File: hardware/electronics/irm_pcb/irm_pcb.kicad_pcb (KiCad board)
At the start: 2 copper layers, 64 parts, among them IC1 23LC1024, J1 Conn_01x04, J10 Conn_02x05_Counter_Clockwise, J11 Conn_01x04, J12 Conn_01x06, J13 Conn_01x06, J14 Conn_01x10, J16 Screw_Terminal_01x02, J17 Conn_01x06, J2 JUMPER_OPEN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

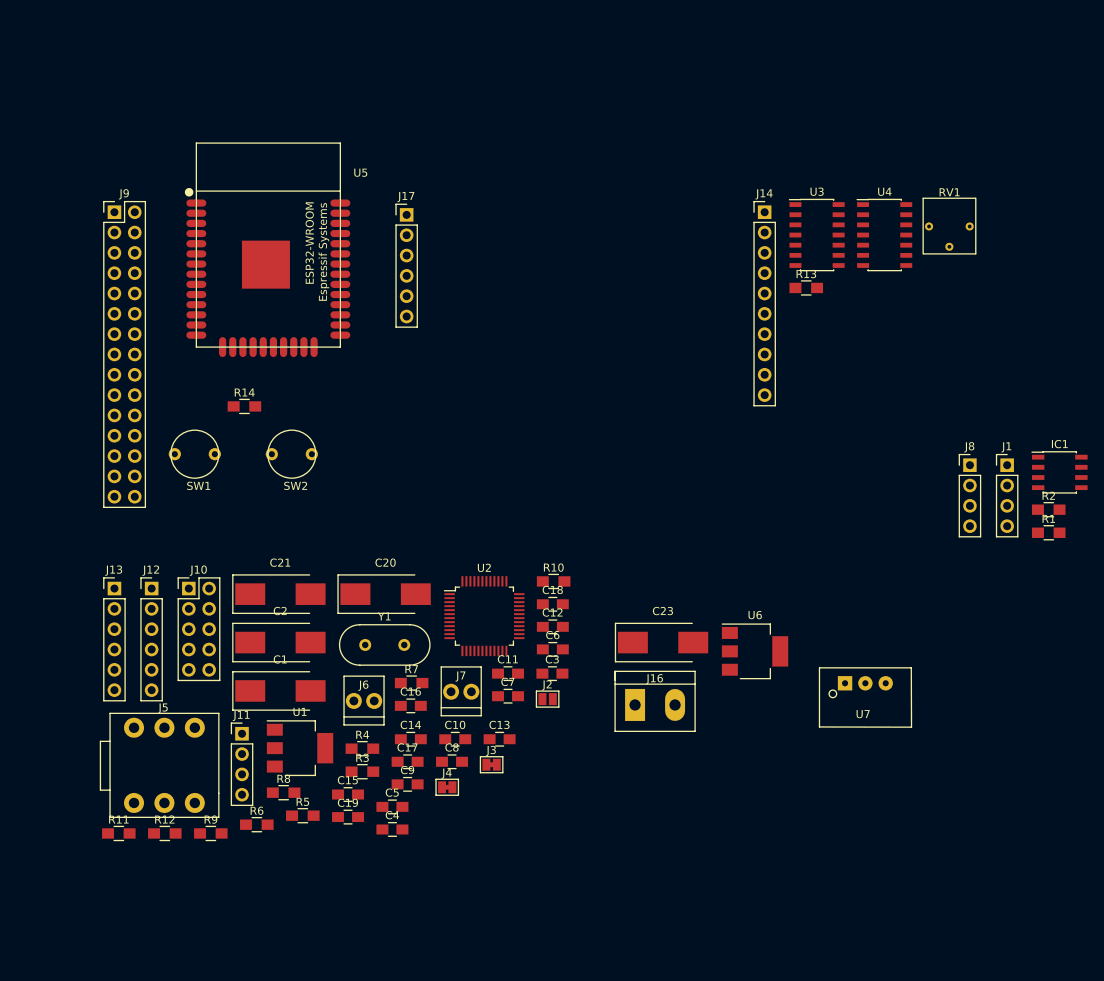
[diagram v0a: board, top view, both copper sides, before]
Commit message: New borad layout - routing incomplete
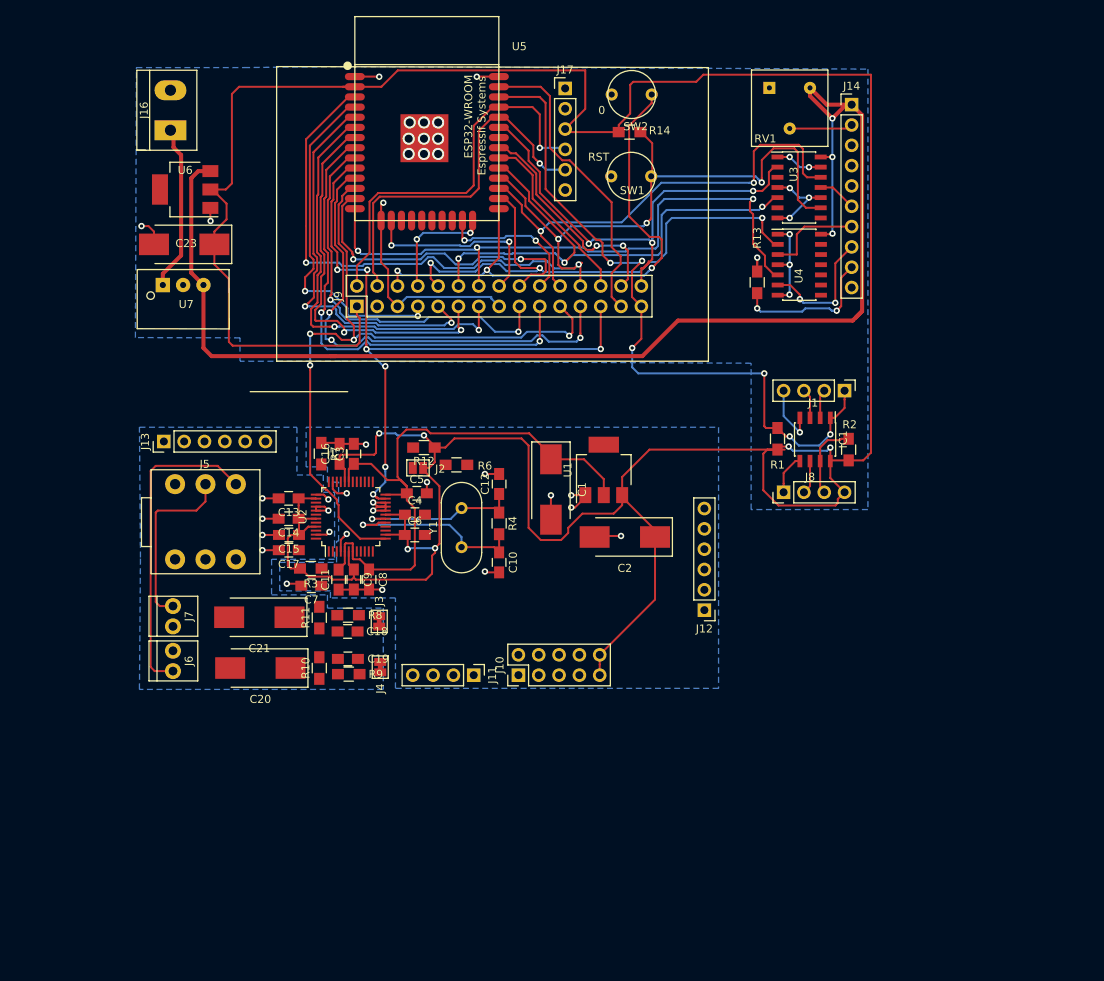
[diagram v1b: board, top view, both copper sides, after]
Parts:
- removed R5: 100K, Resistors_SMD:R_0805_HandSoldering
- RV1: footprint irm_pcb:Potentiometer_Trimmer_Bourns_3339H_Horizontal -> irm_pcb:Potentiometer_Trimmer_Bourns_3386F
- moved U7 98.7 mm to (84.3, 43.1)
- moved J16 95.8 mm to (84.6, 21.2), turned to 90 degrees
- moved U6 91.7 mm to (87.1, 31.1), turned to 180 degrees
- moved C23 77.9 mm to (87.0, 38.0), turned to 180 degrees
- moved J12 69.1 mm to (152.0, 83.7), turned to 180 degrees
- moved SW1 64.7 mm to (142.9, 29.5)
- moved SW2 61.9 mm to (142.9, 19.2)
- moved R14 59.1 mm to (142.7, 23.9)
- moved R12 58.1 mm to (117.0, 63.4), turned to 180 degrees
- moved U1 51.5 mm to (139.4, 66.2), turned to 90 degrees
- moved R6 51.4 mm to (121.0, 65.5), turned to 180 degrees
- moved C2 45.0 mm to (142.1, 74.5), turned to 180 degrees
- moved J10 42.6 mm to (128.8, 91.8), turned to 90 degrees
- moved C1 42.2 mm to (132.8, 68.6), turned to 270 degrees
- moved C13 40.0 mm to (100.1, 69.7), turned to 180 degrees
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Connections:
- net Net-(J16-Pad1) renamed +24V
- J7 pad 1: AGND -> /MP3 Codec/R_OUT
- J7 pad 2: /MP3 Codec/R_OUT -> AGND
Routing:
- net +3V3: track 0.00 -> 420.3 mm, vias 0 -> 6
- net +5V: track 0.00 -> 169.4 mm, vias 0 -> 3
- net /Control/EN: track 0.00 -> 137.2 mm, vias 0 -> 5
- net AGND: track 0.00 -> 136.2 mm, vias 0 -> 45
- net /MP3 Codec/XDCS: track 0.00 -> 91.4 mm, vias 0 -> 4
- net /Buffer RAM/RAM-CS: track 0.00 -> 88.4 mm, vias 0 -> 7
- net /MP3 Codec/XCS: track 0.00 -> 84.7 mm, vias 0 -> 7
- net /Control/RS: track 0.00 -> 77.5 mm, vias 0 -> 3
- net +1.8V: track 0.00 -> 75.9 mm
- net /WROOM Processor/IO0: track 0.00 -> 68.9 mm, vias 0 -> 3
- net /Control/D5: track 0.00 -> 68.3 mm, vias 0 -> 3
- net /Control/D6: track 0.00 -> 66.9 mm, vias 0 -> 3
- net /Control/D4: track 0.00 -> 61.1 mm, vias 0 -> 2
- net /MP3 Codec/DREQ: track 0.00 -> 60.5 mm, vias 0 -> 3
- net /WROOM Processor/IO32: track 0.00 -> 59.8 mm, vias 0 -> 2
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- added copper zone on B.Cu, net AGND
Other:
- net class Power added: clearance 0.2, trace_width 0.508, via_dia 1.524, via_drill 0.762
- board text added: "0"
- board text added: "RST"

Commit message: Routing completed
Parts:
- moved C17 35.5 mm to (101.1, 111.7)
- moved R13 35.4 mm to (168.0, 76.9), turned to 180 degrees
- moved C13 31.7 mm to (104.8, 101.0)
- moved J5 31.6 mm to (95.0, 103.8)
- moved C23 31.6 mm to (93.6, 68.9)
- moved U4 31.6 mm to (168.4, 71.8), turned to 90 degrees
- moved R3 31.5 mm to (107.6, 109.7)
- moved J10 31.5 mm to (134.7, 122.7)
- moved C1 31.5 mm to (138.8, 99.5)
- moved C11 31.5 mm to (112.3, 110.8)
- moved C12 31.5 mm to (132.3, 98.8)
- moved C21 31.5 mm to (102.4, 115.5)
- moved C4 31.5 mm to (121.8, 102.7)
- moved C5 31.5 mm to (122.0, 100.0)
- moved C7 31.5 mm to (108.9, 111.6)
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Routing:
- net +3V3: track 420.3 -> 523.4 mm, vias 6 -> 7
- net /MP3 Codec/DREQ: track 60.5 -> 137.1 mm, vias 3 -> 7
- net /MP3 Codec/RX: track 0.00 -> 73.4 mm, vias 0 -> 4
- net /MP3 Codec/GPIO1: track 0.00 -> 72.0 mm, vias 0 -> 7
- net /MP3 Codec/RIGHT: track 0.00 -> 69.8 mm, vias 0 -> 5
- net /MP3 Codec/LEFT: track 0.00 -> 69.4 mm, vias 0 -> 3
- net /MP3 Codec/TX: track 0.00 -> 60.6 mm, vias 0 -> 6
- net /MP3 Codec/GPIO0: track 0.00 -> 56.3 mm, vias 0 -> 7
- net /MP3 Codec/GPIO2: track 0.00 -> 54.0 mm, vias 0 -> 7
- net /MP3 Codec/SO: track 0.00 -> 54.0 mm, vias 0 -> 4
- net /MP3 Codec/SI: track 0.00 -> 50.5 mm, vias 0 -> 4
- net /MP3 Codec/SCK: track 0.00 -> 50.3 mm, vias 0 -> 4
- net /MP3 Codec/MP3RST: track 0.00 -> 49.0 mm, vias 0 -> 4
- net /MP3 Codec/GPIO3: track 0.00 -> 45.1 mm, vias 0 -> 3
- net /MP3 Codec/LROUT/GPIO4: track 0.00 -> 38.1 mm, vias 0 -> 4
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- added copper zone on F.Cu, net +3V3
- added copper zone on F.Cu, net +5V
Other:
- net class D_Signal added: clearance 0.2, trace_width 0.2, via_dia 0.6, via_drill 0.3

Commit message: Layout completed
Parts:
- moved C23 11.6 mm to (82.0, 68.9)
- moved J16 11.6 mm to (79.0, 52.1)
- moved U7 11.6 mm to (78.7, 74.0)
- moved U6 11.6 mm to (81.5, 62.0)
- moved IC1 8.93 mm to (178.4, 99.4)
- moved R2 8.93 mm to (182.5, 100.6)
- moved J8 8.93 mm to (174.4, 106.0)
- moved R1 8.93 mm to (173.7, 99.3)
- moved J1 8.93 mm to (182.0, 93.3)
- moved J14 7.17 mm to (183.6, 51.7)
- moved R13 7.17 mm to (175.2, 77.2)
- moved RV1 7.17 mm to (175.8, 49.6)
- moved U3 7.17 mm to (175.7, 62.1)
- moved U4 7.17 mm to (175.6, 72.0)
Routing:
- net +3V3: track 523.4 -> 671.0 mm
- net /Buffer RAM/RAM-CS: track 88.5 -> 103.3 mm
- net +5V: track 145.0 -> 158.3 mm
- net /Control/D6: track 76.4 -> 83.5 mm
- net /Control/RS: track 79.5 -> 86.6 mm
- net /Control/D5: track 72.7 -> 79.5 mm
- net /Control/D7: track 58.2 -> 64.1 mm
- net /Control/D4: track 51.9 -> 56.6 mm
- net /MP3 Codec/XCS: track 122.4 -> 118.3 mm
- net /Control/EN: track 131.5 -> 135.2 mm, vias 6 -> 7
- net /MP3 Codec/RX: track 73.4 -> 72.0 mm
- net /MP3 Codec/GPIO1: track 72.0 -> 70.7 mm
- net /WROOM Processor/SENSOR_VP: track 43.5 -> 42.4 mm
- net /WROOM Processor/SENSOR_VN: track 49.6 -> 48.6 mm
- net /MP3 Codec/DREQ: track 137.1 -> 136.4 mm
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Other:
- board outline added: 128 x 81.3 mm
- board text added: "1"
- board text added: "12"
- board text added: "13"
- board text added: "14"
- board text added: "15"
- board text added: "16"
- board text added: "17"
- board text added: "18"
- board text added: "19"
- board text added: "2"
- board text added: "21"
- board text added: "22"
- board text added: "23"
- board text added: "24V"
- board text added: "25"
- board text added: "26"
- board text added: "27"
- board text added: "3"
- board text added: "32"
- board text added: "33"
- board text added: "34"
- board text added: "35"
- board text added: "3V3"
- board text added: "4"
- board text added: "5"
- board text added: "5V"
- board text added: "ANALOG"
- board text added: "CONTRAST"
- board text added: "CONTROL"
- board text added: "D4"
- board text added: "D5"
- board text added: "D6"
- board text added: "D7"
- board text added: "DIGITAL"
- board text added: "DREQ"
- board text added: "EN"
- board text added: "GBUF"
- board text added: "GND"
- board text added: "I2S"
- board text added: "L"
- board text added: "LEFT"
- board text added: "LINE1"
- board text added: "LINE2"
- board text added: "LROUT"
- board text added: "MCLK"
- board text added: "MICN"
- board text added: "NC"
- board text added: "R"
- board text added: "RIGHT"
- board text added: "RS"
- board text added: "RX"
- board text added: "SCK"
- board text added: "SCLK"
- board text added: "SDATA"
- board text added: "SI"
- board text added: "SO"
- board text added: "S_VN"
- board text added: "S_VP"
- board text added: "TX"
- board text added: "XCS"
- board text added: "XDCS"
